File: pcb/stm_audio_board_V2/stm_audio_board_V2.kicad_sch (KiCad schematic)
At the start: 113 parts, among them J1 Power conn, J2 STlink, J3 Audio_sig, J4 Conn_01x10_pots_internal, J5 SPI, J6 Conn_01x03_pot_ext, J7 GuitarIN, J8 GuitarOUT_R, J9 GuitarOUT_L, SW1 SW_SPST, U1 STM32H730VBTx, U2 AMS1117-3.3, U3 AD1974, U4 OP275, U5 AMS1117-3.3, U6 AD1934, U7 OP275, Y2 X1E0000210132

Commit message: Schematic divided into pages, Global connectors added
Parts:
- removed 7660S1: ~, Package_SO:SOIC-8_3.9x4.9mm_P1.27mm, symbol stm_audio:7660S
- removed C1, C10, C11, C12, C14, C16, C27, C3, C30, C32, C33, C34, C35, C36, C5, C52, C53, C54, C55, C56, C57, C58, C59, C6, C60, C61, C62, C7, C8, C9: 100nF, Capacitor_SMD:C_0603_1608Metric_Pad1.08x0.95mm_HandSolder, symbol Device:C_Small
- removed C13, C15: 2.2uF, Capacitor_SMD:C_0805_2012Metric_Pad1.18x1.45mm_HandSolder, symbol Device:C_Polarized_Small_US
- removed C17, C19, C25, C26, C40, C41, C44, C45: 120p, Capacitor_SMD:C_0603_1608Metric_Pad1.08x0.95mm_HandSolder, symbol Device:C_Small
- removed C18: 100p, Capacitor_SMD:C_0603_1608Metric_Pad1.08x0.95mm_HandSolder, symbol Device:C_Small
- removed C2, C29: 1uF, Capacitor_THT:CP_Radial_D6.3mm_P2.50mm, symbol Device:C_Polarized_Small_US
- removed C20, C22, C42, C46: 4.7uF, Capacitor_SMD:C_0805_2012Metric_Pad1.18x1.45mm_HandSolder, symbol Device:C_Polarized_Small_US
- removed C21, C23: 1nF, Capacitor_SMD:C_0603_1608Metric_Pad1.08x0.95mm_HandSolder, symbol Device:C_Small
- removed C24: 100pF, Capacitor_SMD:C_0603_1608Metric_Pad1.08x0.95mm_HandSolder, symbol Device:C_Small
- removed C28, C4: 100uF, Capacitor_THT:CP_Radial_D6.3mm_P2.50mm, symbol Device:C_Polarized_Small_US
- removed C31, C37: 7pF, Capacitor_SMD:C_0603_1608Metric_Pad1.08x0.95mm_HandSolder, symbol Device:C
- removed C38: 5.6nF, Capacitor_SMD:C_0603_1608Metric_Pad1.08x0.95mm_HandSolder, symbol Device:C_Small
- removed C39: 390pF, Capacitor_SMD:C_0603_1608Metric_Pad1.08x0.95mm_HandSolder, symbol Device:C_Small
- removed C43, C47: 2.2nF, Capacitor_SMD:C_0603_1608Metric_Pad1.08x0.95mm_HandSolder, symbol Device:C_Small
- removed C48: 10uF, Capacitor_THT:CP_Radial_D6.3mm_P2.50mm, symbol Device:C_Polarized_Small_US
- removed C49, C50, C64: 10uF, Capacitor_SMD:C_1210_3225Metric_Pad1.33x2.70mm_HandSolder, symbol Device:C_Polarized_Small_US
- removed C51, C63: 100uF, Capacitor_SMD:C_1210_3225Metric_Pad1.33x2.70mm_HandSolder, symbol Device:C_Polarized_Small_US
- removed D1, D4: 1N4148, Diode_THT:D_DO-35_SOD27_P7.62mm_Horizontal, symbol Diode:1N4148
- removed D2: LED, LED_SMD:LED_SK6805_PLCC4_2.4x2.7mm_P1.3mm, symbol Device:LED
- removed D5: 1N914WT, Diode_SMD:D_SOD-523, symbol Diode:1N914WT
- removed H1, H2, H3, H4: MountingHole_Pad, MountingHole:MountingHole_3.2mm_M3, symbol Mechanical:MountingHole_Pad
- removed J1: Power conn, Connector_PinHeader_2.54mm:PinHeader_1x02_P2.54mm_Vertical, symbol Connector_Generic:Conn_01x02
- removed J2: STlink, Connector_PinHeader_2.54mm:PinHeader_1x04_P2.54mm_Vertical, symbol Connector_Generic:Conn_01x04
- removed J3: Audio_sig, Connector_PinHeader_2.54mm:PinHeader_1x03_P2.54mm_Vertical, symbol Connector_Generic:Conn_01x03
- removed J4: Conn_01x10_pots_internal, Connector_PinHeader_2.54mm:PinHeader_1x10_P2.54mm_Vertical, symbol Connector_Generic:Conn_01x10
- removed J5: SPI, Connector_PinHeader_2.54mm:PinHeader_1x03_P2.54mm_Vertical, symbol Connector_Generic:Conn_01x03
- removed J6: Conn_01x03_pot_ext, Connector_PinHeader_2.54mm:PinHeader_1x03_P2.54mm_Vertical, symbol Connector_Generic:Conn_01x03
- removed J7: GuitarIN, Connector_PinHeader_2.54mm:PinHeader_1x01_P2.54mm_Vertical, symbol Connector_Generic:Conn_01x01
- removed J8: GuitarOUT_R, Connector_PinHeader_2.54mm:PinHeader_1x01_P2.54mm_Vertical, symbol Connector_Generic:Conn_01x01
- removed J9: GuitarOUT_L, Connector_PinHeader_2.54mm:PinHeader_1x01_P2.54mm_Vertical, symbol Connector_Generic:Conn_01x01
- removed R1: 330R, Resistor_SMD:R_0805_2012Metric_Pad1.20x1.40mm_HandSolder, symbol Device:R
- removed R10, R4, R5, R6, R7: 5.76k, Resistor_SMD:R_0805_2012Metric_Pad1.20x1.40mm_HandSolder, symbol Device:R
- removed R12: 562, Resistor_SMD:R_0805_2012Metric_Pad1.20x1.40mm_HandSolder, symbol Device:R
- removed R13, R14, R19, R20: 3.32k, Resistor_SMD:R_0805_2012Metric_Pad1.20x1.40mm_HandSolder, symbol Device:R
- removed R15, R16, R21, R22: 4.99k, Resistor_SMD:R_0805_2012Metric_Pad1.20x1.40mm_HandSolder, symbol Device:R
- removed R17, R23: 604, Resistor_SMD:R_0805_2012Metric_Pad1.20x1.40mm_HandSolder, symbol Device:R
- removed R18, R24: 49.9k, Resistor_SMD:R_0805_2012Metric_Pad1.20x1.40mm_HandSolder, symbol Device:R
- removed R2: 10k, Resistor_SMD:R_0805_2012Metric_Pad1.20x1.40mm_HandSolder, symbol Device:R
- removed R8, R9: 237R, Resistor_SMD:R_0805_2012Metric_Pad1.20x1.40mm_HandSolder, symbol Device:R
- removed SW1: SW_SPST, Button_Switch_SMD:SW_SPST_TL3305A, symbol Switch:SW_SPST
- removed U1: STM32H730VBTx, Package_QFP:LQFP-100_14x14mm_P0.5mm, symbol MCU_ST_STM32H7:STM32H730VBTx
- removed U2, U5: AMS1117-3.3, Package_TO_SOT_SMD:SOT-223-3_TabPin2, symbol Regulator_Linear:AMS1117-3.3
- removed U3: AD1974, Package_QFP:LQFP-48_7x7mm_P0.5mm, symbol stm_audio:AD1974
- removed U4, U7: OP275, Package_SO:SSOP-8_3.9x5.05mm_P1.27mm, symbol Amplifier_Operational:OP275
- removed U6: AD1934, Package_QFP:LQFP-48_7x7mm_P0.5mm, symbol stm_audio:AD1934
- removed Y2: X1E0000210132, Crystal:Crystal_SMD_SeikoEpson_TSX3225-4Pin_3.2x2.5mm_HandSoldering, symbol Device:Crystal_GND24_Small
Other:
- added sheet Connectors (Connectors.kicad_sch)
- added sheet Input_stage (Input_stage.kicad_sch)
- added sheet MCU (MCU.kicad_sch)
- added sheet Output_stage (Output_stage.kicad_sch)
- added sheet Power (Power.kicad_sch)
- added sheet display (display.kicad_sch)
- added sheet filters (filters.kicad_sch)
- added sheet potentiometers (potentiometers.kicad_sch)
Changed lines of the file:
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@@
 (kicad_sch (version 20230121) (generator eeschema)
   (paper "A2")
+  (label "+3.3V" (at 72.39 26.67 0) (fields_autoplaced)
+    (effects (font (size 1.27 1.27)) (justify left bottom))
+  )
+  (sheet (at 21.59 36.83) (size 57.15 22.86) (fields_autoplaced)
+    (stroke (width 0.1524) (type solid))
+    (fill (color 0 0 0 0.0000))
+    (property "Sheetname" "Power" (at 21.59 36.1184 0)
+      (effects (font (size 1.27 1.27)) (justify left bottom))
+    )
+    (property "Sheetfile" "Power.kicad_sch" (at 21.59 60.2746 0)
+      (effects (font (size 1.27 1.27)) (justify left top))
+    )
+    (property "Field2" "" (at 21.59 36.83 0)
+      (effects (font (size 1.27 1.27)) hide)
+    )
+    (instances
+      (project "stm_audio_board_V2"
+        (path "/6997cf63-2615-4e49-9471-e7da1b6bae71" (page "2"))
+      )
+    )
+  )
+  (sheet (at 21.59 71.12) (size 57.15 20.32) (fields_autoplaced)
+    (stroke (width 0.1524) (type solid))
+    (fill (color 0 0 0 0.0000))
+    (property "Sheetname" "MCU" (at 21.59 70.4084 0)
+      (effects (font (size 1.27 1.27)) (justify left bottom))
+    )
+    (property "Sheetfile" "MCU.kicad_sch" (at 21.59 92.0246 0)
+      (effects (font (size 1.27 1.27)) (justify left top))
+    )
+    (property "Field2" "" (at 21.59 71.12 0)
+      (effects (font (size 1.27 1.27)) hide)
+    )
+    (instances
+      (project "stm_audio_board_V2"
+        (path "/6997cf63-2615-4e49-9471-e7da1b6bae71" (page "3"))
+      )
+    )
+  )
+  (sheet (at 101.6 143.51) (size 66.04 21.59) (fields_autoplaced)
+    (stroke (width 0.1524) (type solid))
+    (fill (color 0 0 0 0.0000))
+    (property "Sheetname" "Connectors" (at 101.6 142.7984 0)
+      (effects (font (size 1.27 1.27)) (justify left bottom))
+    )
+    (property "Sheetfile" "Connectors.kicad_sch" (at 101.6 165.6846 0)
+      (effects (font (size 1.27 1.27)) (justify left top))
+    )
+    (instances
+      (project "stm_audio_board_V2"
+        (path "/6997cf63-2615-4e49-9471-e7da1b6bae71" (page "8"))
+      )
+    )
+  )
+  (sheet (at 22.86 143.51) (size 59.69 22.86) (fields_autoplaced)
+    (stroke (width 0.1524) (type solid))
+    (fill (color 0 0 0 0.0000))
+    (property "Sheetname" "Output_stage" (at 22.86 142.7984 0)
+      (effects (font (size 1.27 1.27)) (justify left bottom))
+    )
+    (property "Sheetfile" "Output_stage.kicad_sch" (at 22.86 166.9546 0)
+      (effects (font (size 1.27 1.27)) (justify left top))
+    )
+    (instances
+      (project "stm_audio_board_V2"
+        (path "/6997cf63-2615-4e49-9471-e7da1b6bae71" (page "5"))
+      )
+    )
+  )
+  (sheet (at 22.86 177.8) (size 46.99 12.7) (fields_autoplaced)
+    (stroke (width 0.1524) (type solid))
+    (fill (color 0 0 0 0.0000))
+    (property "Sheetname" "filters" (at 22.86 177.0884 0)
+      (effects (font (size 1.27 1.27)) (justify left bottom))
+    )
+    (property "Sheetfile" "filters.kicad_sch" (at 22.86 191.0846 0)
+      (effects (font (size 1.27 1.27)) (justify left top))
+    )
+    (property "Field2" "" (at 22.86 177.8 0)
+      (effects (font (size 1.27 1.27)) hide)
+    )
+    (instances
+      (project "stm_audio_board_V2"
+        (path "/6997cf63-2615-4e49-9471-e7da1b6bae71" (page "9"))
+      )
+    )
+  )
+  (sheet (at 102.87 72.39) (size 43.18 20.32) (fields_autoplaced)
+    (stroke (width 0.1524) (type solid))
+    (fill (color 0 0 0 0.0000))
+    (property "Sheetname" "display" (at 102.87 71.6784 0)
+      (effects (font (size 1.27 1.27)) (justify left bottom))
+    )
+    (property "Sheetfile" "display.kicad_sch" (at 102.87 93.2946 0)
+      (effects (font (size 1.27 1.27)) (justify left top))
+    )
+    (instances
+      (project "stm_audio_board_V2"
+        (path "/6997cf63-2615-4e49-9471-e7da1b6bae71" (page "7"))
+      )
+    )
+  )
+  (sheet (at 21.59 105.41) (size 52.07 22.86) (fields_autoplaced)
+    (stroke (width 0.1524) (type solid))
+    (fill (color 0 0 0 0.0000))
+    (property "Sheetname" "Input_stage" (at 21.59 104.6984 0)
+      (effects (font (size 1.27 1.27)) (justify left bottom))
+    )
+    (property "Sheetfile" "Input_stage.kicad_sch" (at 21.59 128.8546 0)
+      (effects (font (size 1.27 1.27)) (justify left top))
+    )
+    (instances
+      (project "stm_audio_board_V2"
+        (path "/6997cf63-2615-4e49-9471-e7da1b6bae71" (page "4"))
+      )
+    )
+  )
+  (sheet (at 104.14 41.91) (size 44.45 20.32) (fields_autoplaced)
+    (stroke (width 0.1524) (type solid))
+    (fill (color 0 0 0 0.0000))
+    (property "Sheetname" "potentiometers" (at 104.14 41.1984 0)
+      (effects (font (size 1.27 1.27)) (justify left bottom))
+    )
+    (property "Sheetfile" "potentiometers.kicad_sch" (at 104.14 62.8146 0)
+      (effects (font (size 1.27 1.27)) (justify left top))
+    )
+    (instances
+      (project "stm_audio_board_V2"
+        (path "/6997cf63-2615-4e49-9471-e7da1b6bae71" (page "6"))
+      )
+    )
+  )
+  (sheet_instances
+    (path "/" (page "1"))
+  )
+)

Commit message: pcb design update
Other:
- added sheet codec (codec.kicad_sch)
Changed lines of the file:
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@@
+    )
+  )
+  (sheet (at 97.79 105.41) (size 53.34 25.4) (fields_autoplaced)
+    (stroke (width 0.1524) (type solid))
+    (fill (color 0 0 0 0.0000))
+    (property "Sheetname" "codec" (at 97.79 104.6984 0)
+      (effects (font (size 1.27 1.27)) (justify left bottom))
+    )
+    (property "Sheetfile" "codec.kicad_sch" (at 97.79 131.3946 0)
+      (effects (font (size 1.27 1.27)) (justify left top))
+    )
+    (instances
+      (project "stm_audio_board_V2"
+        (path "/6997cf63-2615-4e49-9471-e7da1b6bae71" (page "10"))
+      )
     )
   )

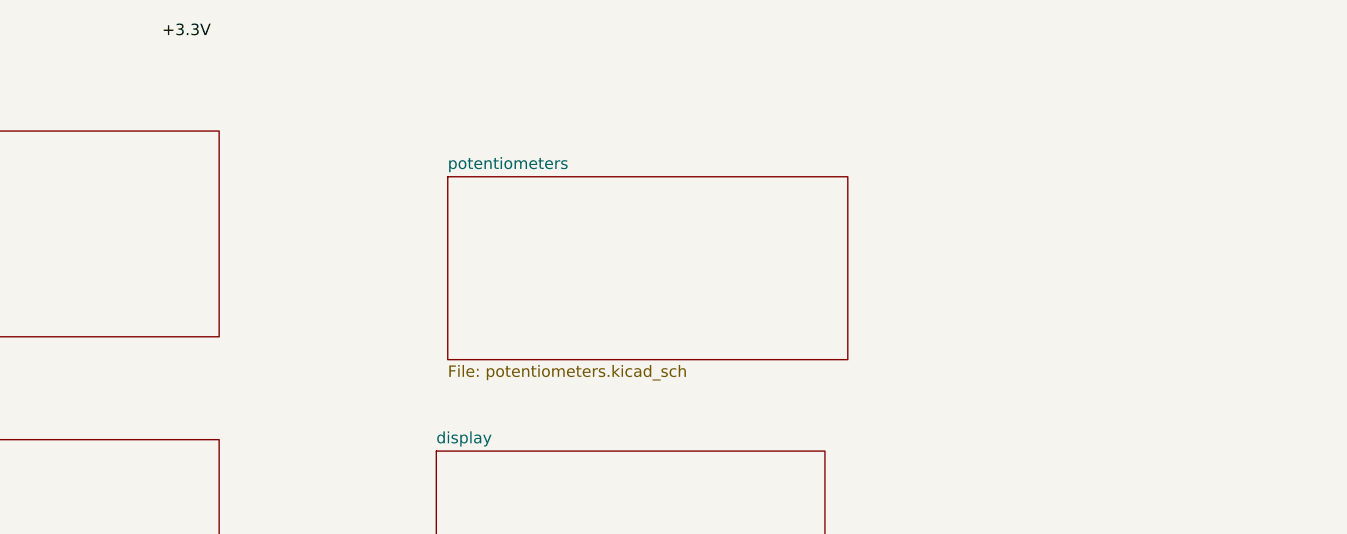
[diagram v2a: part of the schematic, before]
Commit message: input and output stage reworked in sim and in schematic, power filtering is changed, further calculations needed
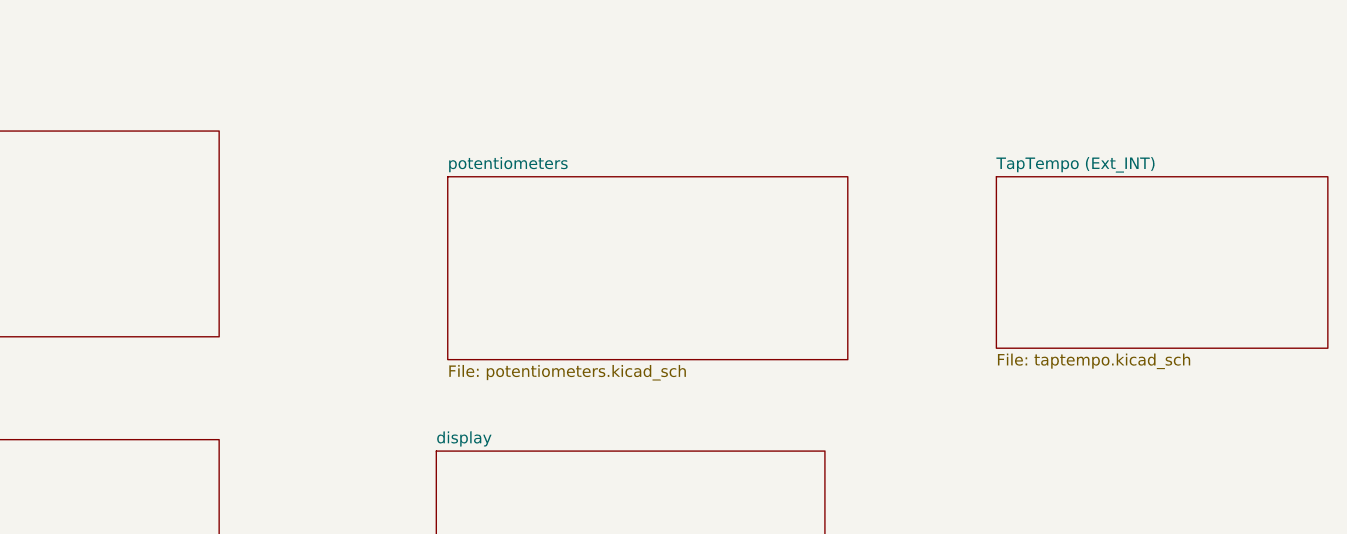
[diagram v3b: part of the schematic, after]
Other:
- added sheet TapTempo (Ext_INT) (taptempo.kicad_sch)
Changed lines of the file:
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@@
 (kicad_sch (version 20230121) (generator eeschema)
   (paper "A2")
-  (label "+3.3V" (at 72.39 26.67 0) (fields_autoplaced)
-    (effects (font (size 1.27 1.27)) (justify left bottom))
-  )
   (sheet (at 21.59 36.83) (size 57.15 22.86) (fields_autoplaced)
     (stroke (width 0.1524) (type solid))
@@
       )
     )
+  )
+  (sheet (at 165.1 41.91) (size 36.83 19.05) (fields_autoplaced)
+    (stroke (width 0.1524) (type solid))
+    (fill (color 0 0 0 0.0000))
+    (property "Sheetname" "TapTempo (Ext_INT)" (at 165.1 41.1984 0)
+      (effects (font (size 1.27 1.27)) (justify left bottom))
+    )
+    (property "Sheetfile" "taptempo.kicad_sch" (at 165.1 61.5446 0)
+      (effects (font (size 1.27 1.27)) (justify left top))
+    )
+    (property "Field2" "" (at 165.1 41.91 0)
+      (effects (font (size 1.27 1.27)) hide)
+    )
+    (property "Field3" "" (at 165.1 41.91 0)
+      (effects (font (size 1.27 1.27)) hide)
+    )
+    (instances
+      (project "stm_audio_board_V2"
+        (path "/6997cf63-2615-4e49-9471-e7da1b6bae71" (page "11"))
+      )
+    )
